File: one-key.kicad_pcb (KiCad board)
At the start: 2 copper layers, 20.5 x 25 mm, 3 parts, among them SW1 SW_SPST

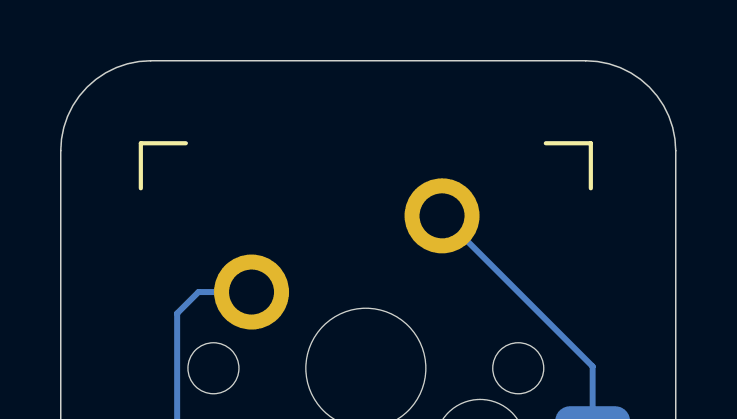
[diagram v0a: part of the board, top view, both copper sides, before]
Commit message: 
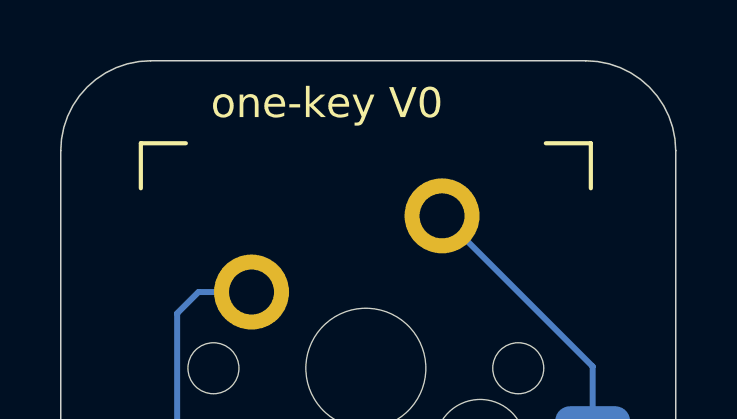
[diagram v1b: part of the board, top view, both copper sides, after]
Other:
- board text added: "one-key V0"
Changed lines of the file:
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@@
 	)
 	(setup
+		(stackup
+			(layer "F.SilkS"
+				(type "Top Silk Screen")
+			)
+			(layer "F.Paste"
+				(type "Top Solder Paste")
+			)
+			(layer "F.Mask"
+				(type "Top Solder Mask")
+				(thickness 0.01)
+			)
+			(layer "F.Cu"
+				(type "copper")
+				(thickness 0.035)
+			)
+			(layer "dielectric 1"
+				(type "core")
+				(thickness 1.51)
+				(material "FR4")
+				(epsilon_r 4.5)
+				(loss_tangent 0.02)
+			)
+			(layer "B.Cu"
+				(type "copper")
+				(thickness 0.035)
+			)
+			(layer "B.Mask"
+				(type "Bottom Solder Mask")
+				(thickness 0.01)
+			)
+			(layer "B.Paste"
+				(type "Bottom Solder Paste")
+			)
+			(layer "B.SilkS"
+				(type "Bottom Silk Screen")
+			)
+			(copper_finish "None")
+			(dielectric_constraints no)
+		)
 		(pad_to_mask_clearance 0)
 		(allow_soldermask_bridges_in_footprints no)
@@
 		(layer "Edge.Cuts")
 	)
+	(gr_text "one-key V0"
+		(at 138 80 0)
+		(layer "F.SilkS")
+		(effects
+			(font
+				(size 1 1)
+				(thickness 0.1)
+			)
+			(justify left bottom)
+		)
+	)
 	(segment

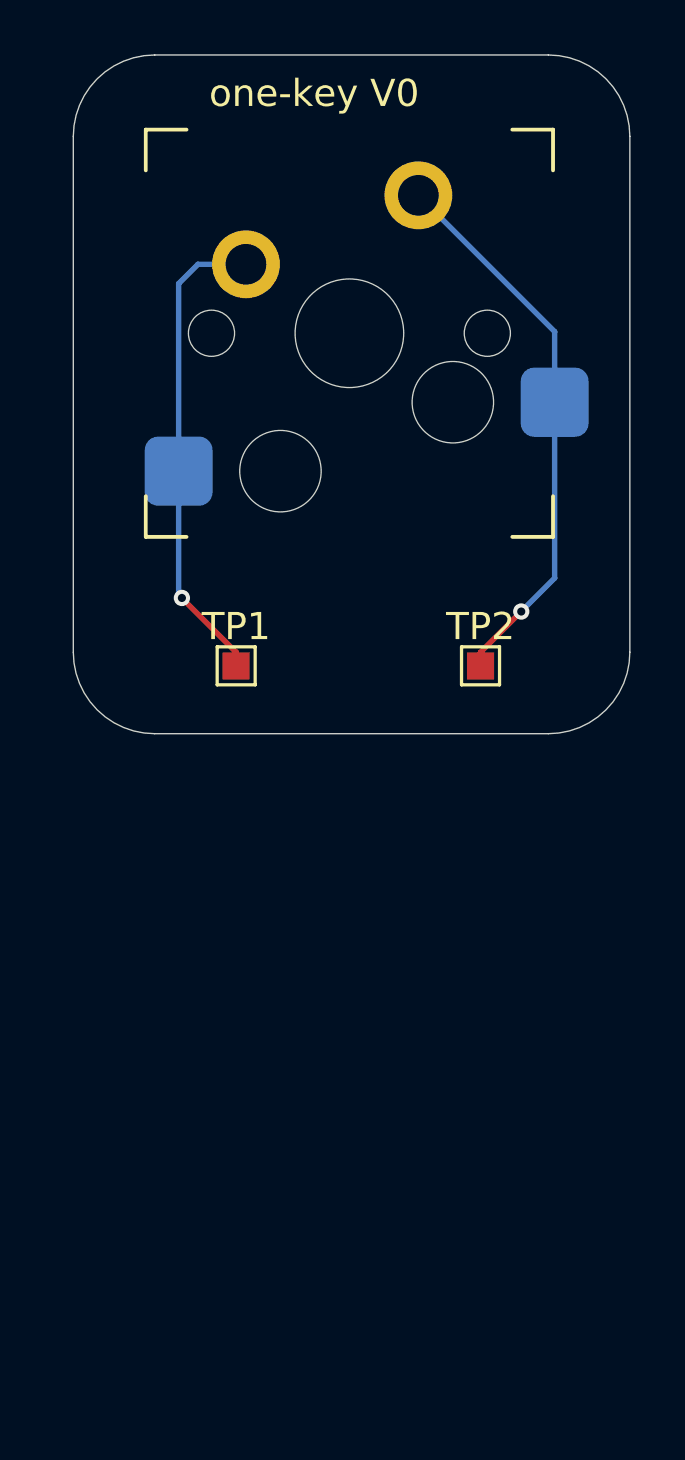
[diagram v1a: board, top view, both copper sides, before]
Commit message: 
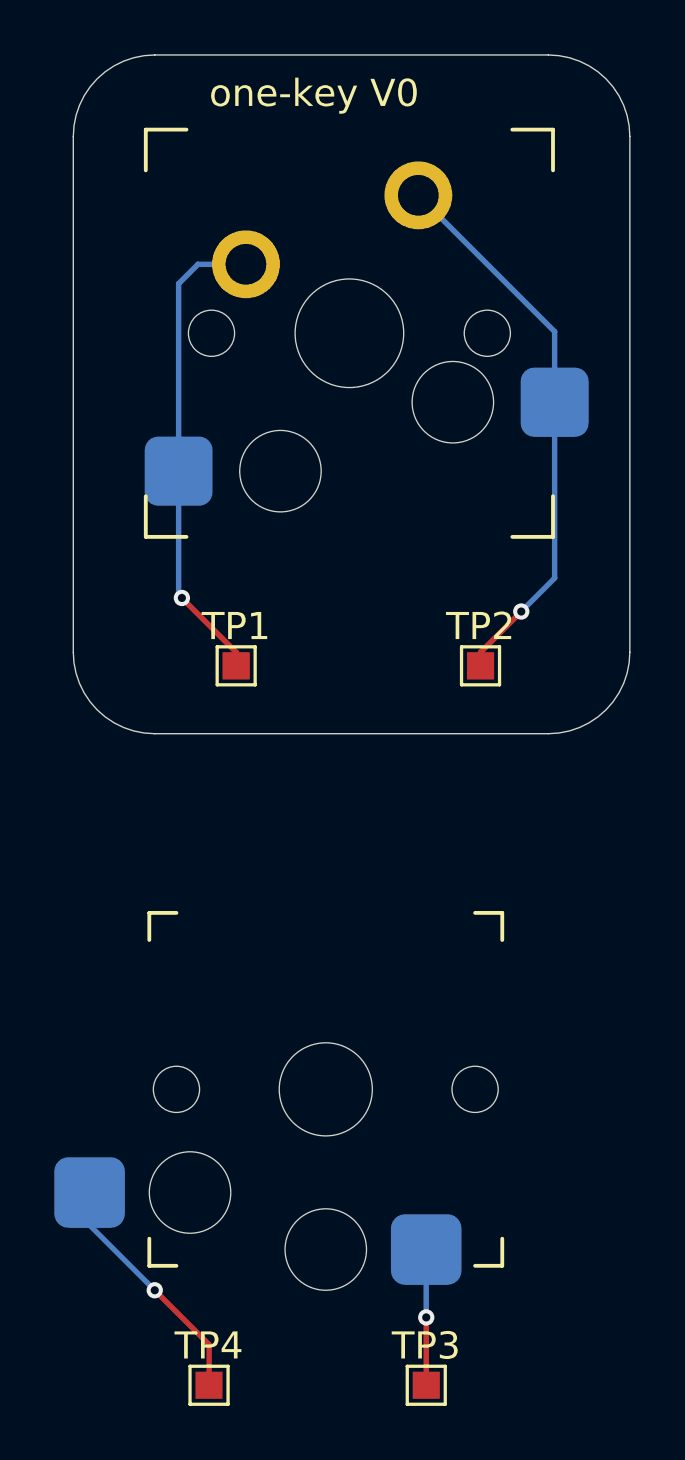
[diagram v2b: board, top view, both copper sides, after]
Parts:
- added SW2: SW_Push, key-switches:SW_Kailh_Choc_V1_HotSwap, F.Cu at (142.3, 116.1)
- added TP3: TestPoint, TestPoint:TestPoint_Pad_1.0x1.0mm, F.Cu at (146.0, 127.0)
- added TP4: TestPoint, TestPoint:TestPoint_Pad_1.0x1.0mm, F.Cu at (138.0, 127.0)
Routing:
- net Net-(SW2-Pad2): track 0.00 -> 8.92 mm, vias 0 -> 1
- net Net-(SW2-Pad1): track 0.00 -> 5.00 mm, vias 0 -> 1
